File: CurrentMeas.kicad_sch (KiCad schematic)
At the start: 72 parts, among them J4 Conn_02x02_Top_Bottom, J5 Conn_02x02_Top_Bottom, J6 Conn_02x02_Top_Bottom, J7 Conn_02x02_Top_Bottom, U28 TMR-3-1223, U31 LMV321, U61 LMV321, U62 LMV321, U63 TLV431, U64 LMV321

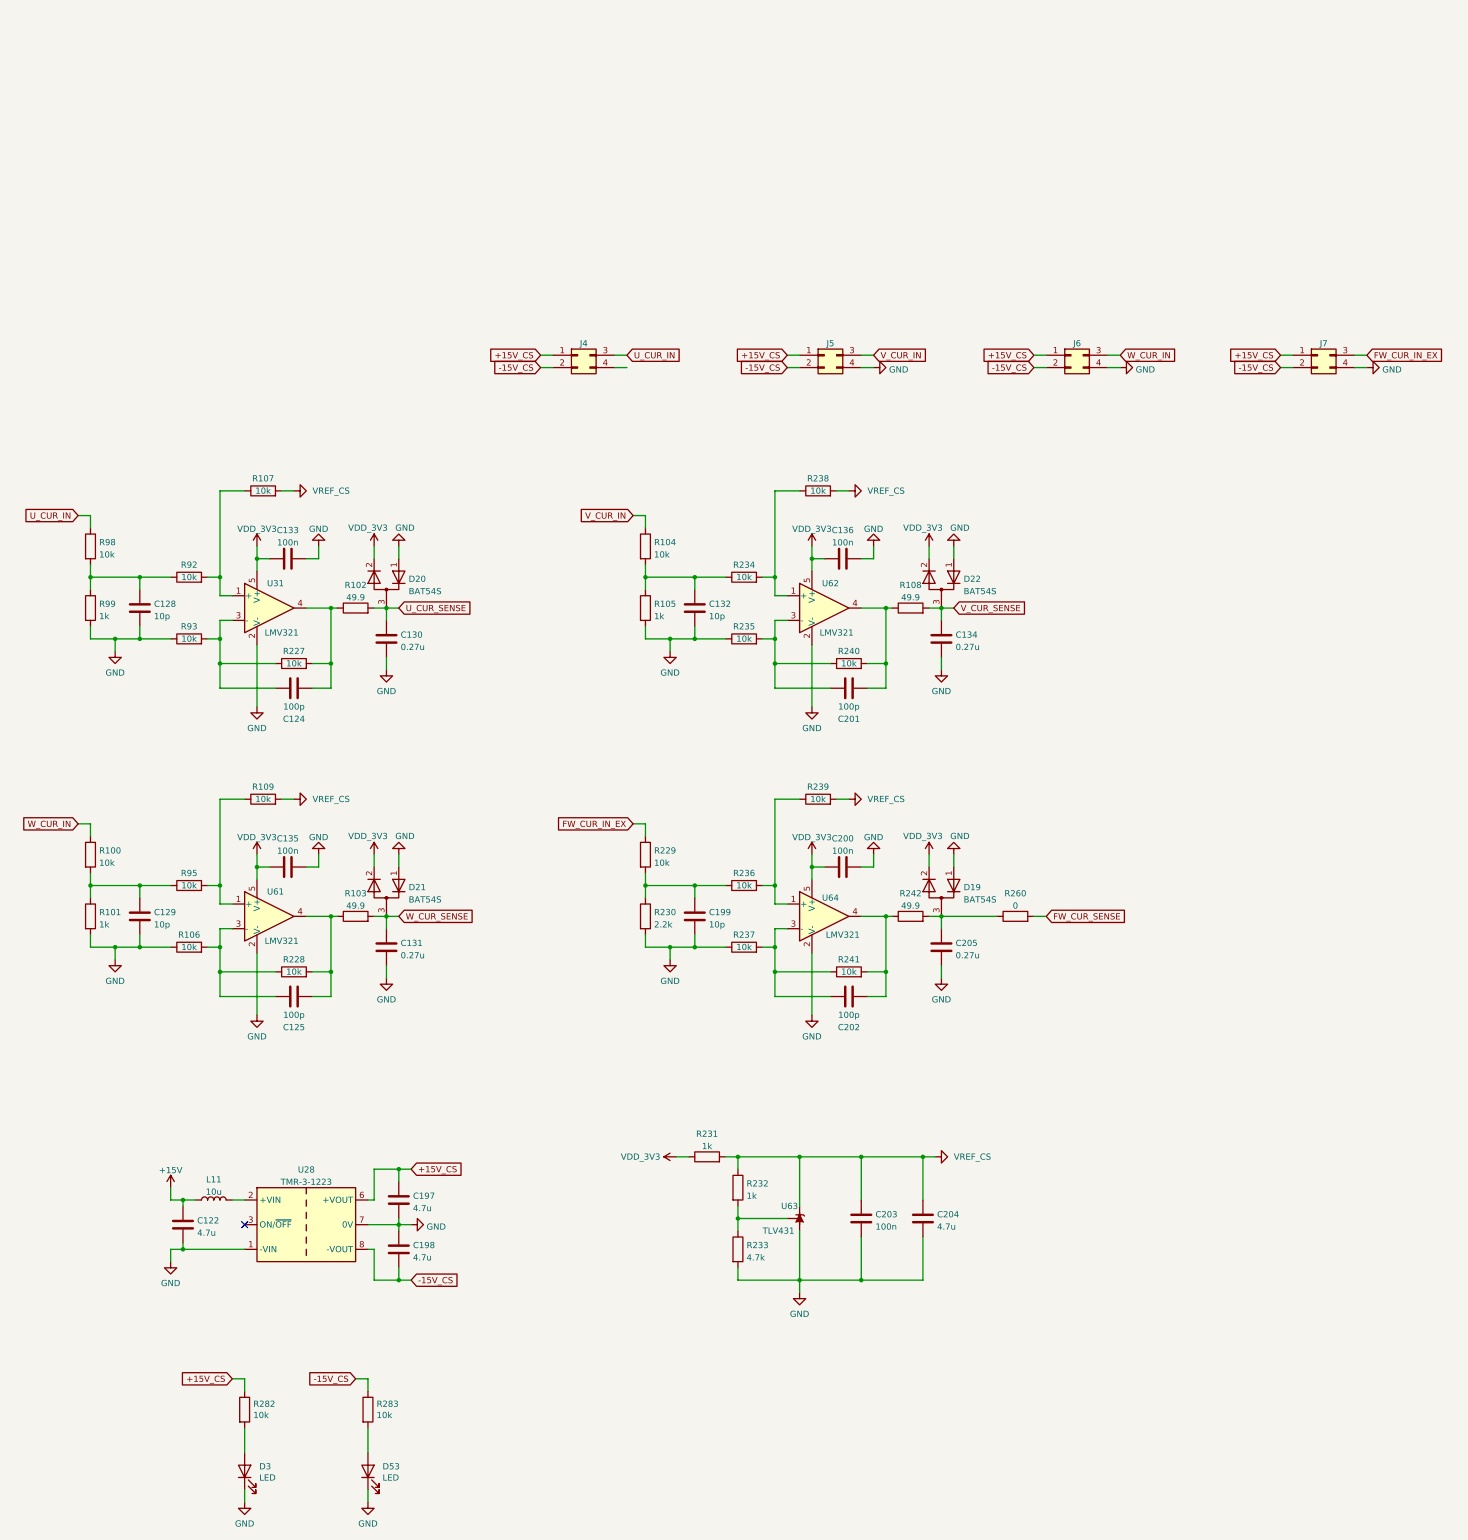
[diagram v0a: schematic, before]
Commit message: Изменения в схеме: убрал разъемы датчиков тока
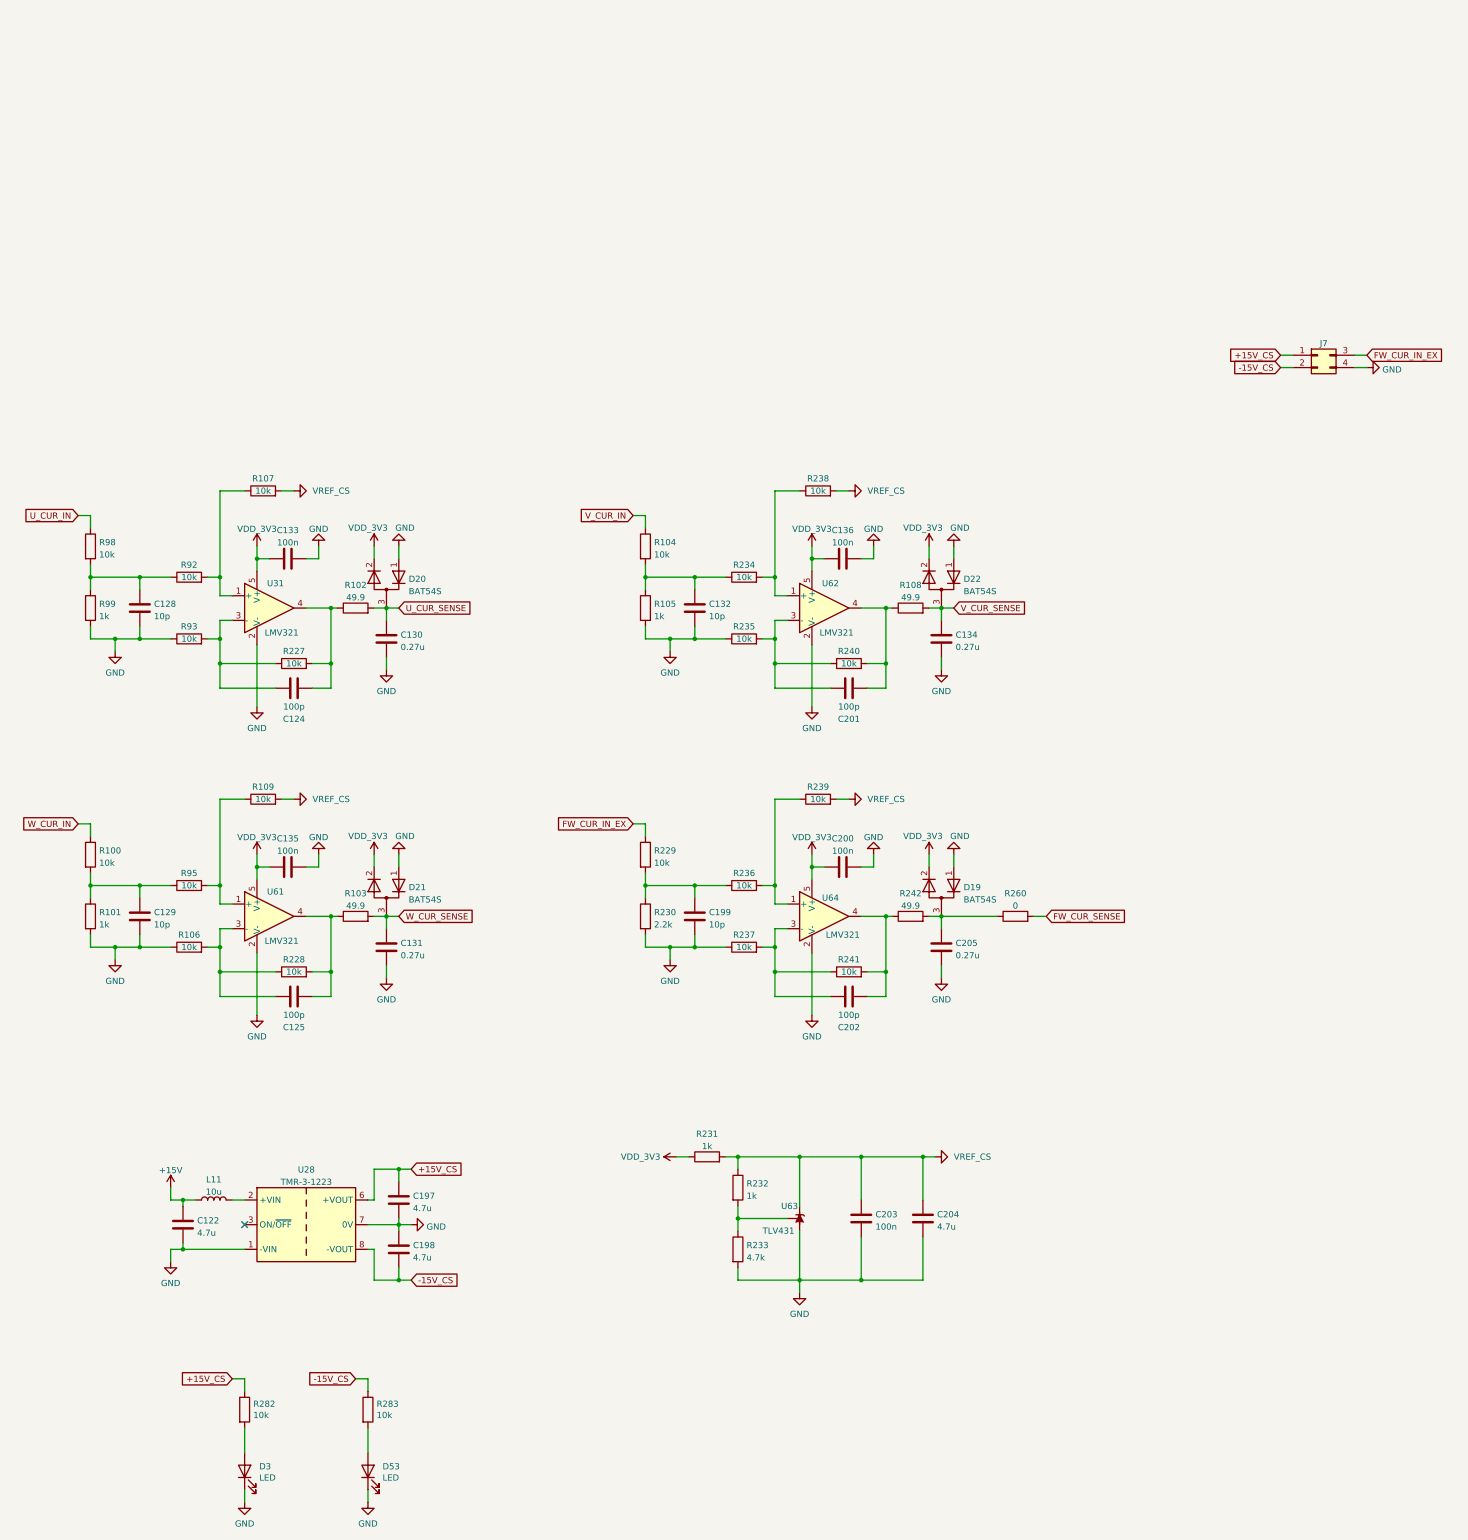
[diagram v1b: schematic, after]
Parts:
- removed J4, J5, J6: Conn_02x02_Top_Bottom, Connector_Molex:Molex_Micro-Fit_3.0_43045-0400_2x02_P3.00mm_Horizontal, symbol Connector_Generic:Conn_02x02_Top_Bottom

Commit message: Изменения в схеме: поменял направление меток
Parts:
- added C241: 10p, Capacitor_SMD:C_0603_1608Metric, symbol Device:C
- added C242: 100n, Capacitor_SMD:C_0603_1608Metric, symbol Device:C
- added C243: 0.27u, Capacitor_SMD:C_0603_1608Metric, symbol Device:C
- added D55: BAT54S, Package_TO_SOT_SMD:SOT-23, symbol Device:D_Dual_Series_AKC_Parallel
- added R305: 10k, Resistor_SMD:R_0603_1608Metric, symbol Device:R
- added R306: 16k, Resistor_SMD:R_0603_1608Metric, symbol Device:R
- added R307: 49.9, Resistor_SMD:R_0603_1608Metric, symbol Device:R
- added R308: 0, Resistor_SMD:R_0603_1608Metric, symbol Device:R
- added U6: LMV321, Package_TO_SOT_SMD:SOT-23-5, symbol Amplifier_Operational:LMV321
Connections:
- net FW_CUR_SENSE: now also R308.2
- net GND: now also C241.2, C242.2, C243.2, D55.1 (K), R306.2, U6.2 (V-)
- net VDD_3V3: now also C242.1, D55.2 (K), U6.5 (V+)
- new net: C241.1, R305.2, R306.1, U6.1 (+)
- new net: R307.1, U6.3 (-), U6.4
- new net: C243.1, D55.3 (A), R307.2, R308.1
- new net FW_CUR_IN_INT: R305.1

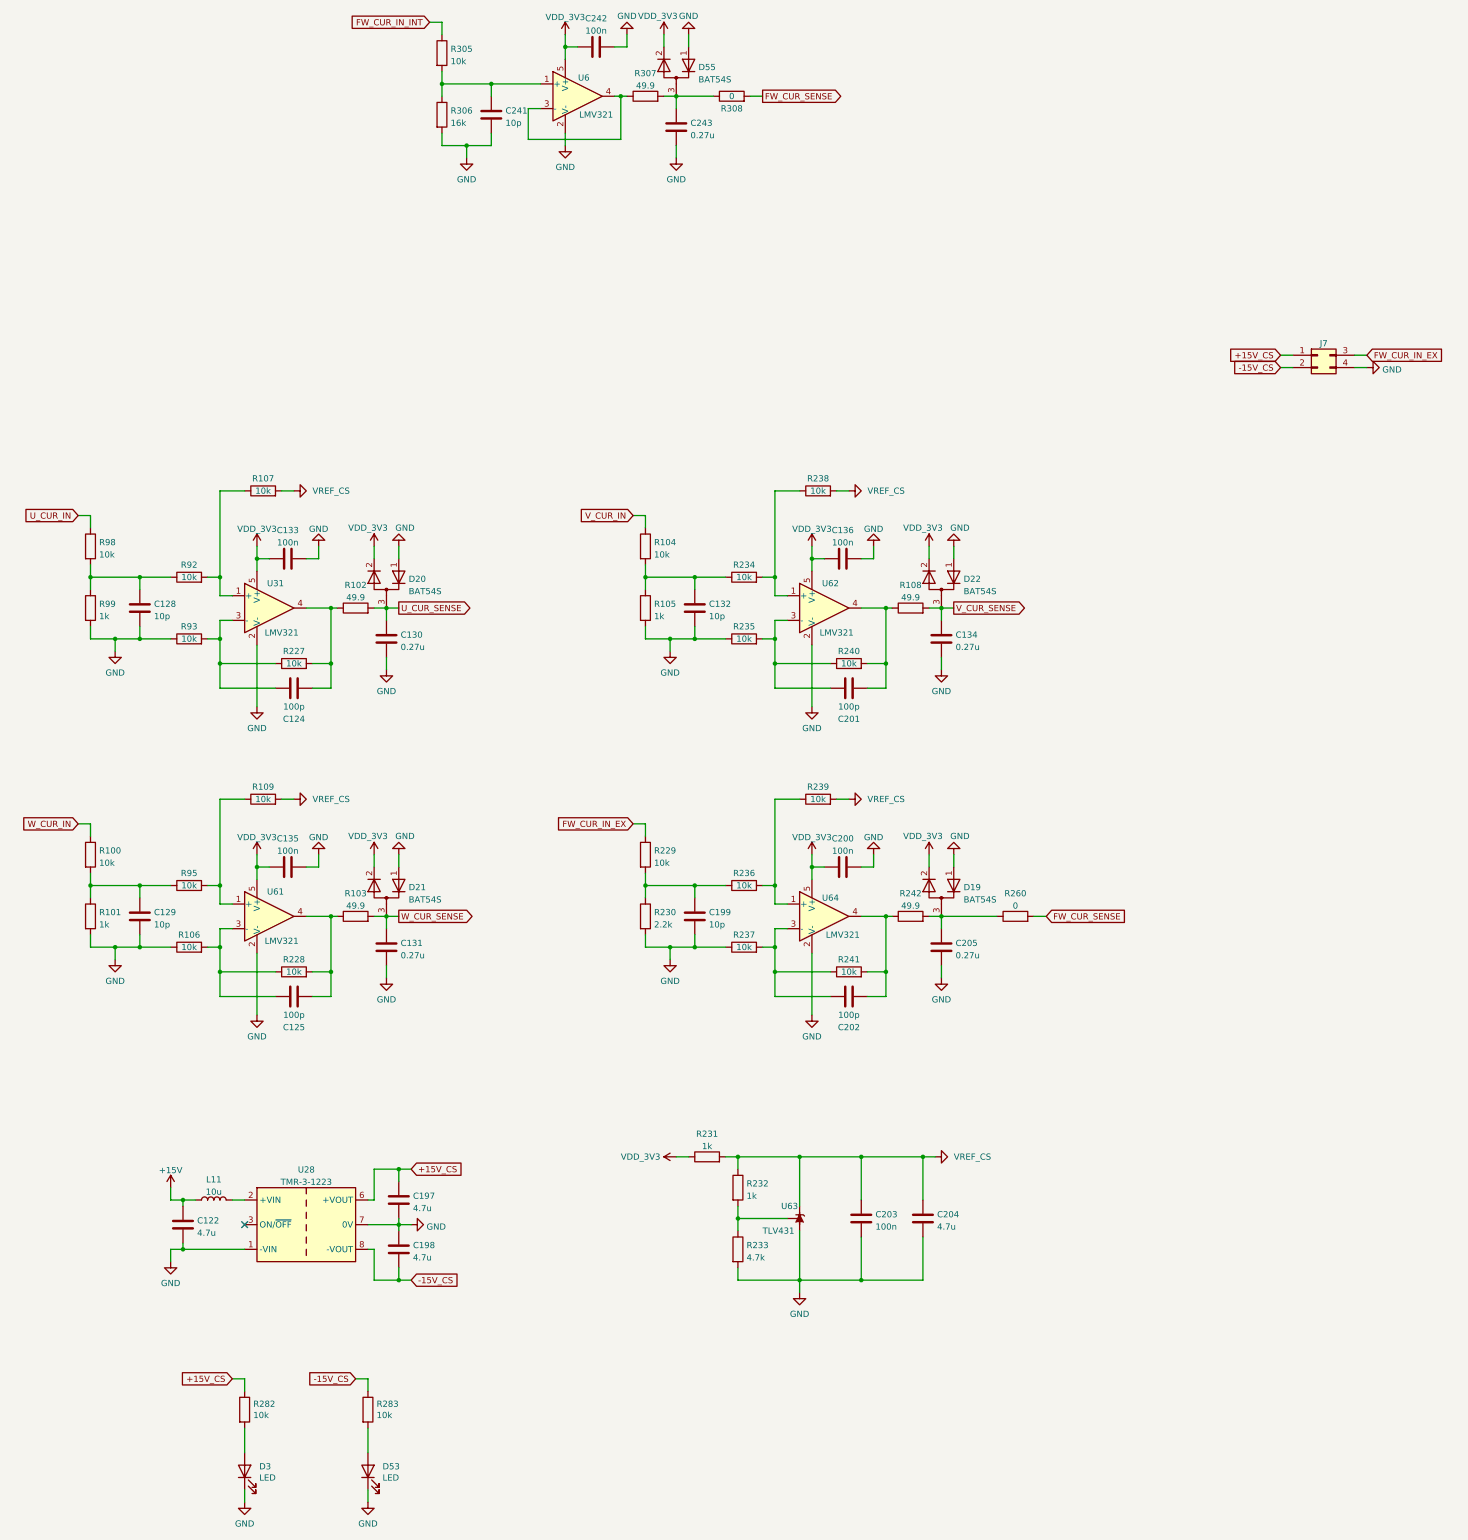
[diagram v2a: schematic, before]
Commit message: Исправление: в схеме добавил обработку температур, изменил обработку токов
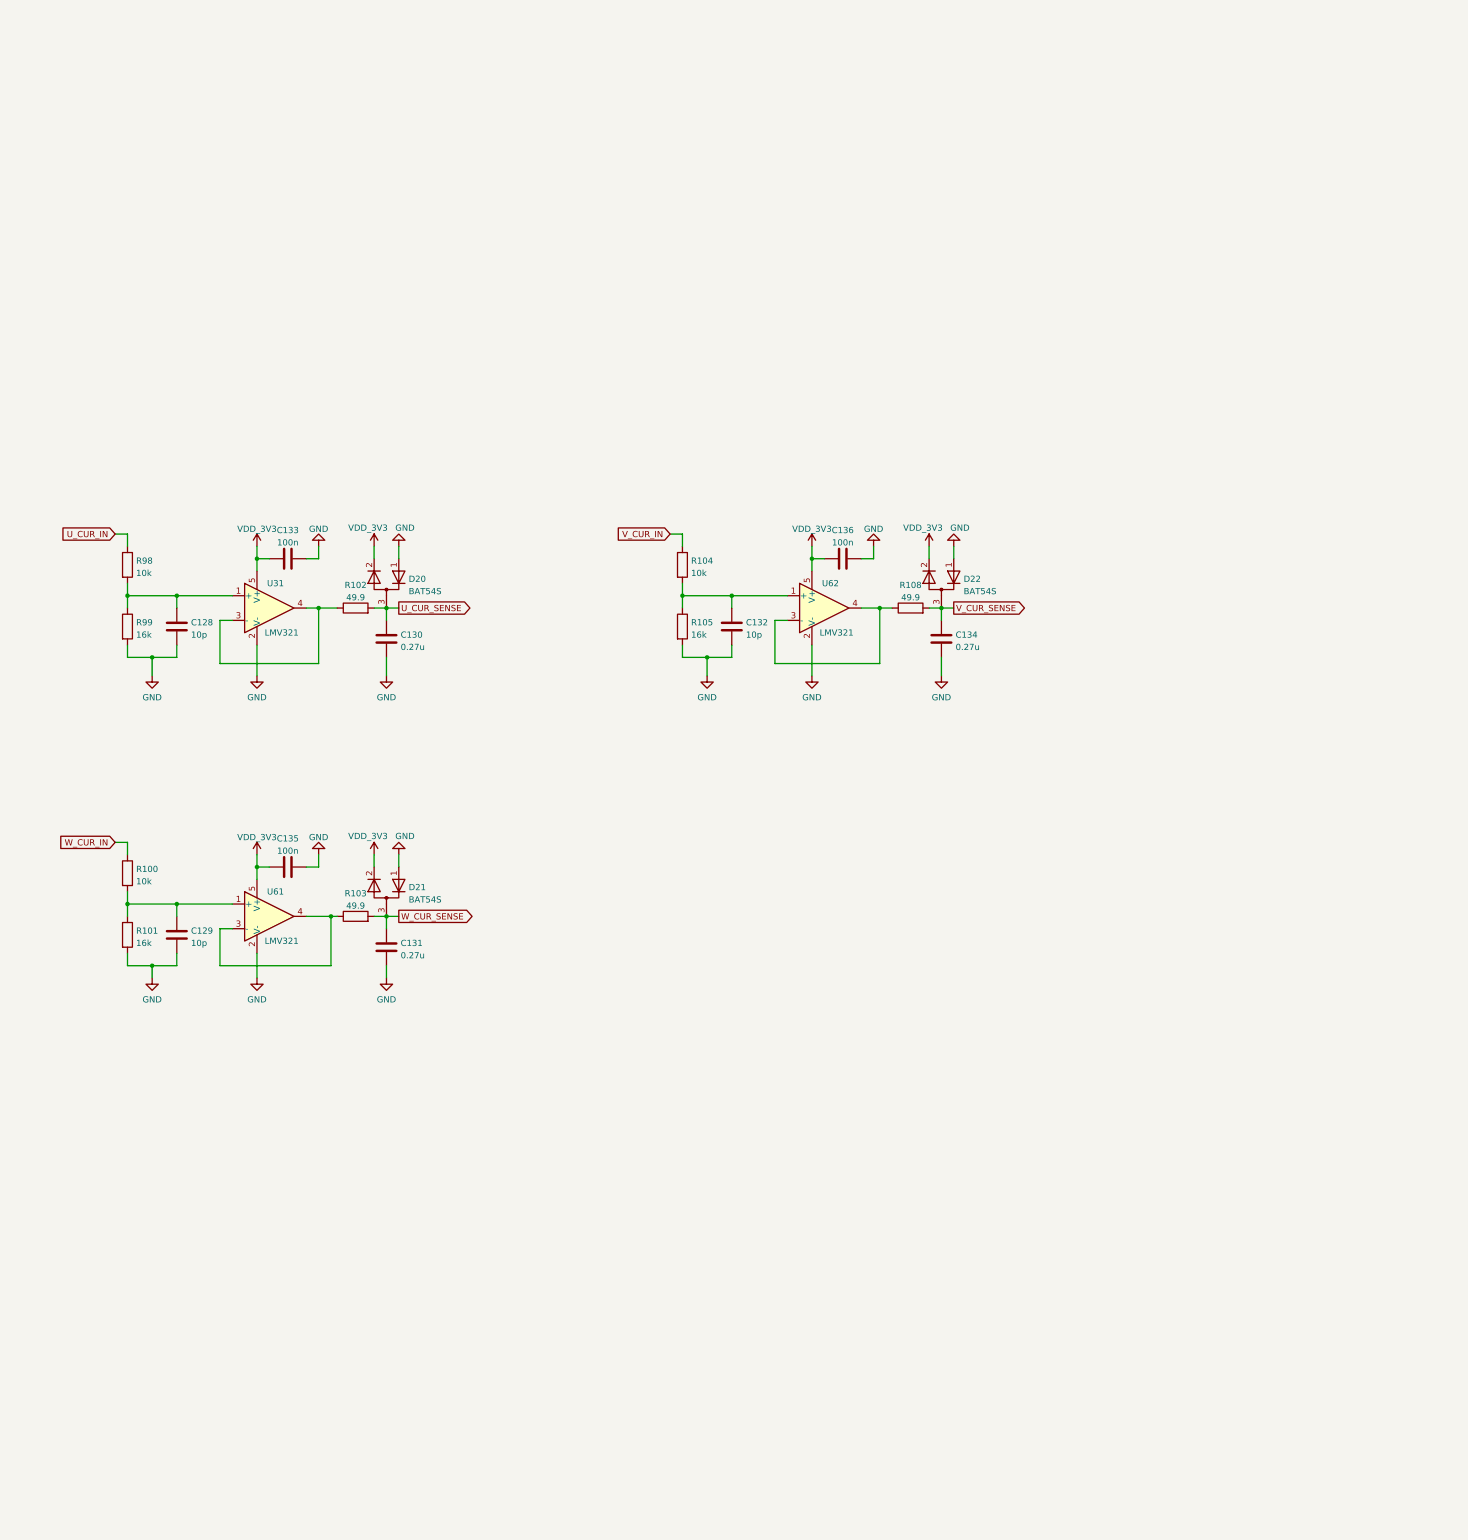
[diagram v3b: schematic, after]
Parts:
- removed C122: 4.7u, Capacitor_SMD:C_1206_3216Metric, symbol Device:C
- removed C124, C125, C201, C202: 100p, Capacitor_SMD:C_0603_1608Metric, symbol Device:C
- removed C197, C198: 4.7u, Capacitor_SMD:C_0805_2012Metric, symbol Device:C
- removed C199, C241: 10p, Capacitor_SMD:C_0603_1608Metric, symbol Device:C
- removed C200, C203, C242: 100n, Capacitor_SMD:C_0603_1608Metric, symbol Device:C
- removed C204: 4.7u, Capacitor_SMD:C_0603_1608Metric, symbol Device:C
- removed C205, C243: 0.27u, Capacitor_SMD:C_0603_1608Metric, symbol Device:C
- removed D19, D55: BAT54S, Package_TO_SOT_SMD:SOT-23, symbol Device:D_Dual_Series_AKC_Parallel
- removed D3, D53: LED, LED_SMD:LED_0805_2012Metric_Pad1.15x1.40mm_HandSolder, symbol Device:LED
- removed J7: Conn_02x02_Top_Bottom, Connector_Molex:Molex_Micro-Fit_3.0_43045-0400_2x02_P3.00mm_Horizontal, symbol Connector_Generic:Conn_02x02_Top_Bottom
- removed L11: 10u, Inductor_SMD:L_1008_2520Metric, symbol Device:L
- removed R106, R107, R109, R227, R228, R229, R234, R235, R236, R237, R238, R239, R240, R241, R305, R92, R93, R95: 10k, Resistor_SMD:R_0603_1608Metric, symbol Device:R
- removed R230: 2.2k, Resistor_SMD:R_0603_1608Metric, symbol Device:R
- removed R231, R232: 1k, Resistor_SMD:R_0603_1608Metric, symbol Device:R
- removed R233: 4.7k, Resistor_SMD:R_0603_1608Metric, symbol Device:R
- removed R242, R307: 49.9, Resistor_SMD:R_0603_1608Metric, symbol Device:R
- removed R260, R308: 0, Resistor_SMD:R_0603_1608Metric, symbol Device:R
- removed R282, R283: 10k, Resistor_SMD:R_0805_2012Metric_Pad1.20x1.40mm_HandSolder, symbol Device:R
- removed R306: 16k, Resistor_SMD:R_0603_1608Metric, symbol Device:R
- removed U28: TMR-3-1223, Project_Library:TMR 3-1223, symbol Project_Library:TMR-3-1223
- removed U6, U64: LMV321, Package_TO_SOT_SMD:SOT-23-5, symbol Amplifier_Operational:LMV321
- removed U63: TLV431, Package_TO_SOT_SMD:SOT-23, symbol My_Library:TLV431
- R101, R105, R99: value 1k -> 16k
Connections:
- net at R102.1, U31.4: now also U31.3 (-)
- net at C128.1, R98.2, R99.1: now also U31.1 (+)
- net at C129.1, R100.2, R101.1: now also U61.1 (+)
- net at U62.3 (-): now also R108.1, U62.4
- net at U61.3 (-): now also R103.1, U61.4
- net at C132.1, R104.2, R105.1: now also U62.1 (+)
- no-connect marks 1 -> 0
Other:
- moved on the sheet: C128, C129, C132, R100, R101, R104, R105, R98, R99
